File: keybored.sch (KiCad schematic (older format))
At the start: 16 parts, among them U1 ATmega32U4-AU, Y1 16MHz

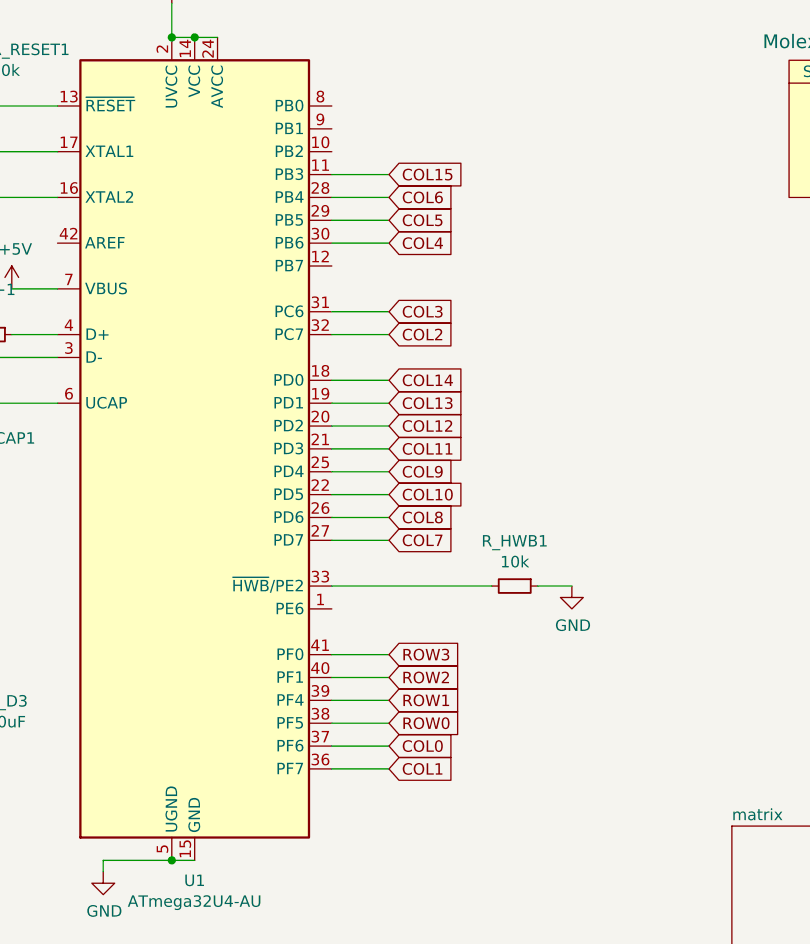
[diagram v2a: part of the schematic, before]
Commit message: moved MCU above ortho48 section
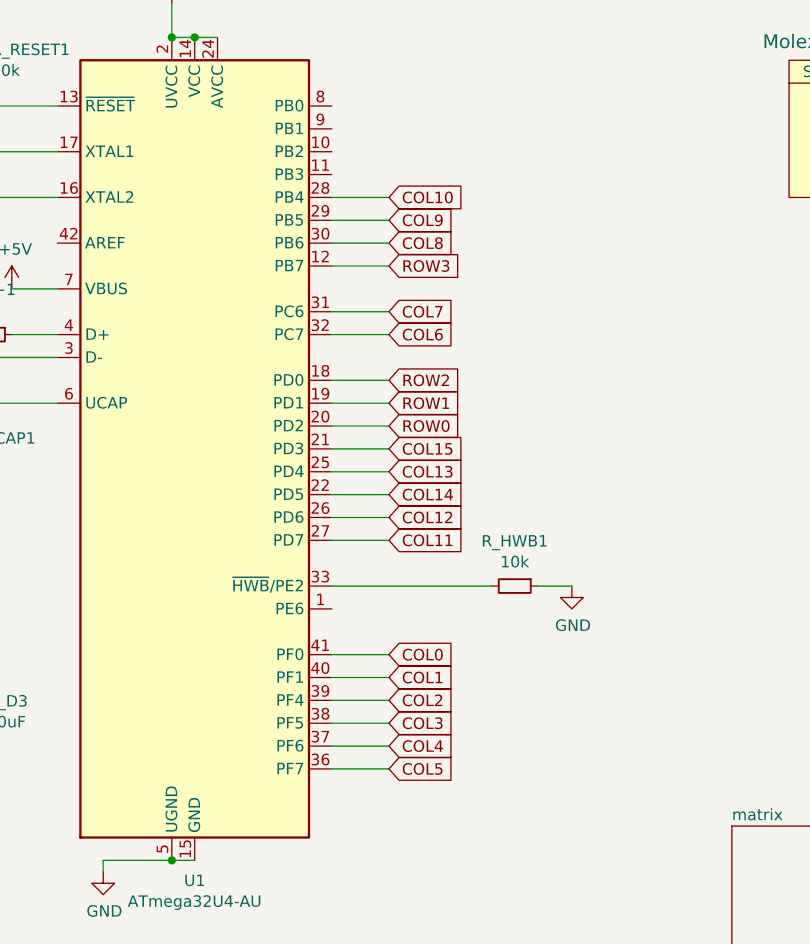
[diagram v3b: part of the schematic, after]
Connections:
- net COL0: now also U1.41 (PF0); no longer U1.37 (PF6)
- net COL1: now also U1.40 (PF1); no longer U1.36 (PF7)
- net COL10: now also U1.28 (PB4); no longer U1.22 (PD5)
- net COL11: now also U1.27 (PD7); no longer U1.21 (PD3)
- net COL12: now also U1.26 (PD6); no longer U1.20 (PD2)
- net COL13: now also U1.25 (PD4); no longer U1.19 (PD1)
- net COL14: now also U1.22 (PD5); no longer U1.18 (PD0)
- net COL15: now also U1.21 (PD3); no longer U1.11 (PB3)
- net COL2: now also U1.39 (PF4); no longer U1.32 (PC7)
- net COL3: now also U1.38 (PF5); no longer U1.31 (PC6)
- net COL4: now also U1.37 (PF6); no longer U1.30 (PB6)
- net COL5: now also U1.36 (PF7); no longer U1.29 (PB5)
- net COL6: now also U1.32 (PC7); no longer U1.28 (PB4)
- net COL7: now also U1.31 (PC6); no longer U1.27 (PD7)
- net COL8: now also U1.30 (PB6); no longer U1.26 (PD6)
- net COL9: now also U1.29 (PB5); no longer U1.25 (PD4)
- net ROW0: now also U1.20 (PD2); no longer U1.38 (PF5)
- net ROW1: now also U1.19 (PD1); no longer U1.39 (PF4)
- net ROW2: now also U1.18 (PD0); no longer U1.40 (PF1)
- net ROW3: now also U1.12 (PB7); no longer U1.41 (PF0)
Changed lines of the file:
@@
 	7150 2150 6850 2150
 Text GLabel 4550 2200 2    50   Input ~ 0
-COL6
+COL10
 Wire Wire Line
 	4550 2300 4300 2300
@@
 $EndSheet
 Text GLabel 4550 2300 2    50   Input ~ 0
+COL9
+Text GLabel 4550 2400 2    50   Input ~ 0
+COL8
+Text GLabel 4550 2700 2    50   Input ~ 0
+COL7
+Text GLabel 4550 2800 2    50   Input ~ 0
+COL6
+Text GLabel 4550 3000 2    50   Input ~ 0
+ROW2
+Text GLabel 4550 3100 2    50   Input ~ 0
+ROW1
+Text GLabel 4550 3200 2    50   Input ~ 0
+ROW0
+Text GLabel 4550 3300 2    50   Input ~ 0
+COL15
+Text GLabel 4550 3400 2    50   Input ~ 0
+COL13
+Text GLabel 4550 3500 2    50   Input ~ 0
+COL14
+Text GLabel 4550 3600 2    50   Input ~ 0
+COL12
+Text GLabel 4550 3700 2    50   Input ~ 0
+COL11
+Text GLabel 4550 4200 2    50   Input ~ 0
+COL0
+Text GLabel 4550 4300 2    50   Input ~ 0
+COL1
+Text GLabel 4550 4400 2    50   Input ~ 0
+COL2
+Text GLabel 4550 4600 2    50   Input ~ 0
+COL4
+Text GLabel 4550 4700 2    50   Input ~ 0
 COL5
-Text GLabel 4550 2400 2    50   Input ~ 0
-COL4
-Text GLabel 4550 2700 2    50   Input ~ 0
-COL3
-Text GLabel 4550 2800 2    50   Input ~ 0
-COL2
-Text GLabel 4550 3000 2    50   Input ~ 0
-COL14
-Text GLabel 4550 3100 2    50   Input ~ 0
-COL13
-Text GLabel 4550 3200 2    50   Input ~ 0
-COL12
-Text GLabel 4550 3300 2    50   Input ~ 0
-COL11
-Text GLabel 4550 3400 2    50   Input ~ 0
-COL9
-Text GLabel 4550 3500 2    50   Input ~ 0
-COL10
-Text GLabel 4550 3600 2    50   Input ~ 0
-COL8
-Text GLabel 4550 3700 2    50   Input ~ 0
-COL7
-Text GLabel 4550 4200 2    50   Input ~ 0
-ROW3
-Text GLabel 4550 4300 2    50   Input ~ 0
-ROW2
-Text GLabel 4550 4400 2    50   Input ~ 0
-ROW1
-Text GLabel 4550 4600 2    50   Input ~ 0
-COL0
-Text GLabel 4550 4700 2    50   Input ~ 0
-COL1
 Wire Wire Line
 	4550 2400 4300 2400
@@
 	4550 4700 4300 4700
 Text GLabel 4550 4500 2    50   Input ~ 0
-ROW0
-Text GLabel 4550 2100 2    50   Input ~ 0
-COL15
+COL3
+Text GLabel 4550 2500 2    50   Input ~ 0
+ROW3
 Wire Wire Line
-	4550 2100 4300 2100
+	4550 2500 4300 2500
 $EndSCHEMATC
